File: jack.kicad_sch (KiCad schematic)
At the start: 9 parts

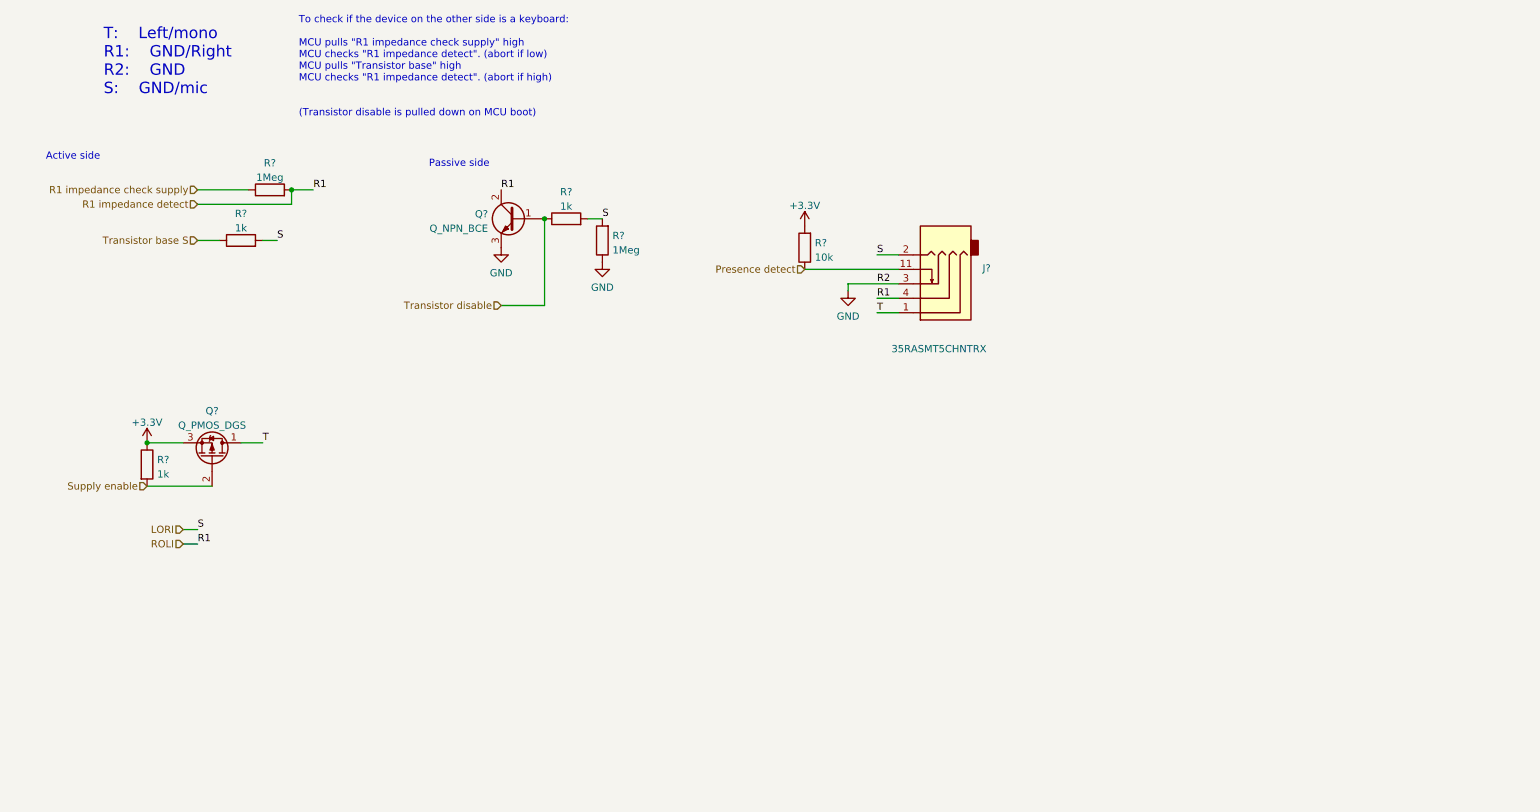
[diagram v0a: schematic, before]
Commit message: Hot pluggable trrs
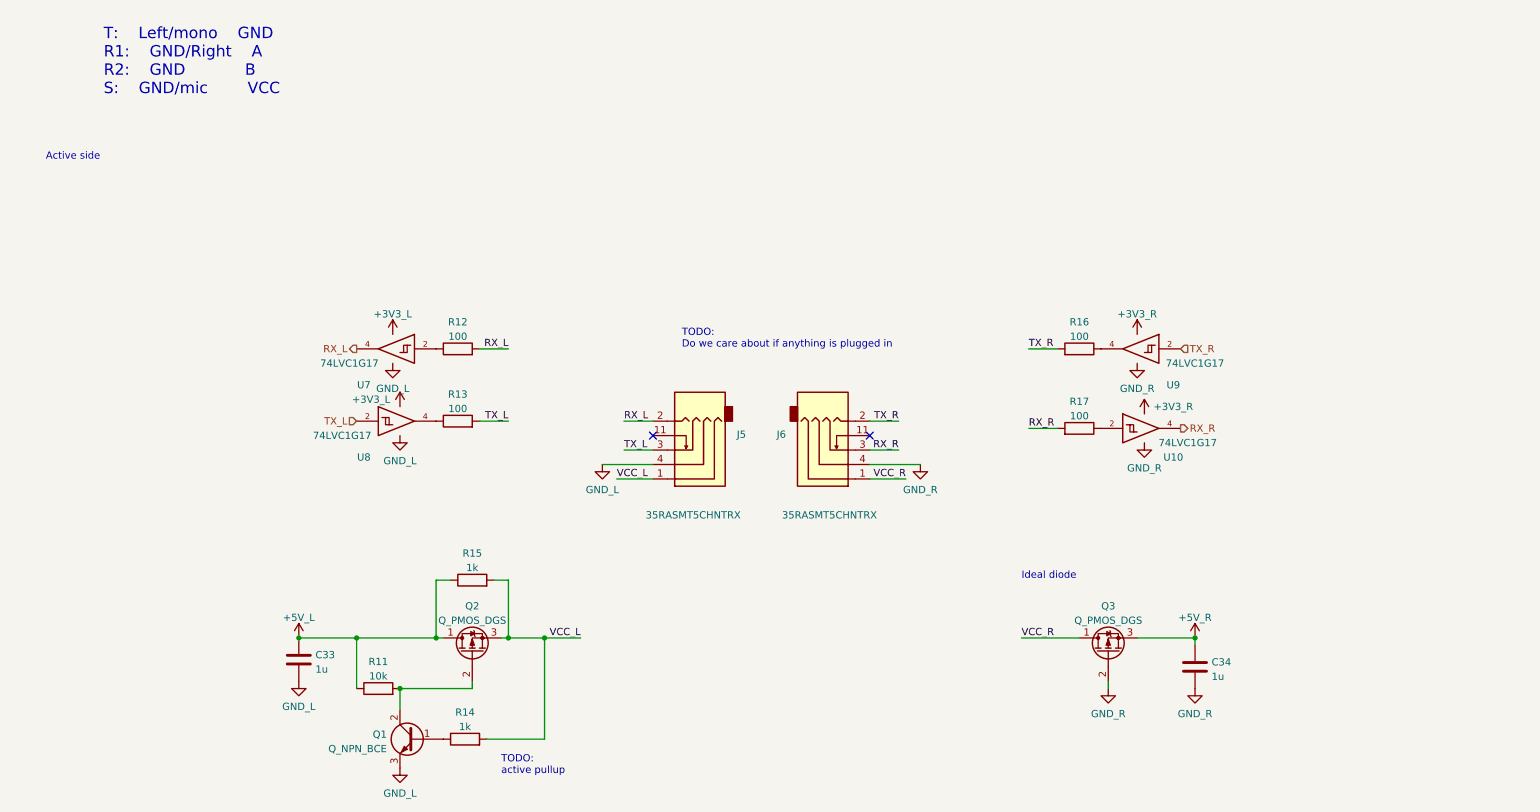
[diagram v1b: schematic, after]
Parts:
- removed Q?: Q_PMOS_DGS, symbol Device:Q_PMOS_DGS
- removed Q?: Q_NPN_BCE, symbol Device:Q_NPN_BCE
- removed R?: 10k, symbol Device:R
- removed R? (x3): 1k, symbol Device:R
- removed R? (x2): 1Meg, symbol Device:R
- added C33, C34: 1u, symbol Device:C
- added J6: 35RASMT5CHNTRX, symbol arisu-split:35RASMT5CHNTRX
- added Q1: Q_NPN_BCE, symbol Device:Q_NPN_BCE
- added Q2, Q3: Q_PMOS_DGS, symbol Device:Q_PMOS_DGS
- added R11: 10k, symbol Device:R
- added R12, R13, R16, R17: 100, symbol Device:R
- added R14, R15: 1k, symbol Device:R
- added U10, U7, U8, U9: 74LVC1G17, symbol 74xGxx:74LVC1G17
- gave numbers to parts that had none: 1
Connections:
- net R1 impedance detect is gone; now on net GND: J5.4
- net GND: now also C33.2, C34.2, J6.4, Q1.3 (E), Q3.2 (G), U10.3 (GND), U7.3 (GND), U8.3 (GND), U9.3 (GND); no longer J5.3
- net LORI renamed RX_L
- net RX_L: now also R12.2, U7.4
- net Presence detect: no longer names the net of J5.11
- net T renamed VCC_L
- net VCC_L: now also Q2.3 (S), R14.2, R15.2
- new net: Q1.1 (B), R14.1
- new net: Q1.2 (C), Q2.2 (G), R11.2
- new net: R16.1, U9.4
- new net: R12.1, U7.2
- new net: R13.1, U8.4
- new net: R17.1, U10.2
- new net +3V3_L: U10.5 (VCC), U7.5 (VCC), U8.5 (VCC), U9.5 (VCC)
- new net +5R: C34.1, Q3.3 (S)
- new net +5V_L: C33.1, Q2.1 (D), R11.1, R15.1
- new net RX_R: J6.3, R17.2, U10.4
- new net TX_L: J5.3, R13.2, U8.2
- new net TX_R: J6.2, R16.2, U9.2
- new net VCC_R: J6.1, Q3.1 (D)
- no-connect marks 0 -> 2
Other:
- note added: "Ideal diode"
- note added: "T: Left/mono GND R1: GND/Right A R2: GND B S: GND/mic VCC"
- note added: "TODO: Do we care about if anything is plugged in"
- note added: "TODO: active pullup"
- note removed: "Passive side"
- note removed: "T: Left/mono R1: GND/Right R2: GND S: GND/mic"
- note removed: "To check if the device on the other side is a keyboard: MCU pulls "R1 impedance check supply" high MCU checks "R1 impedance detect". (abort if low) MCU pulls "Transistor base" high MCU checks "R1 impedance detect". (abort if high) (Transistor disable is pulled down on MCU boot)"
- moved on the sheet: J5

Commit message: No more erc errors + centering and socketing of switches
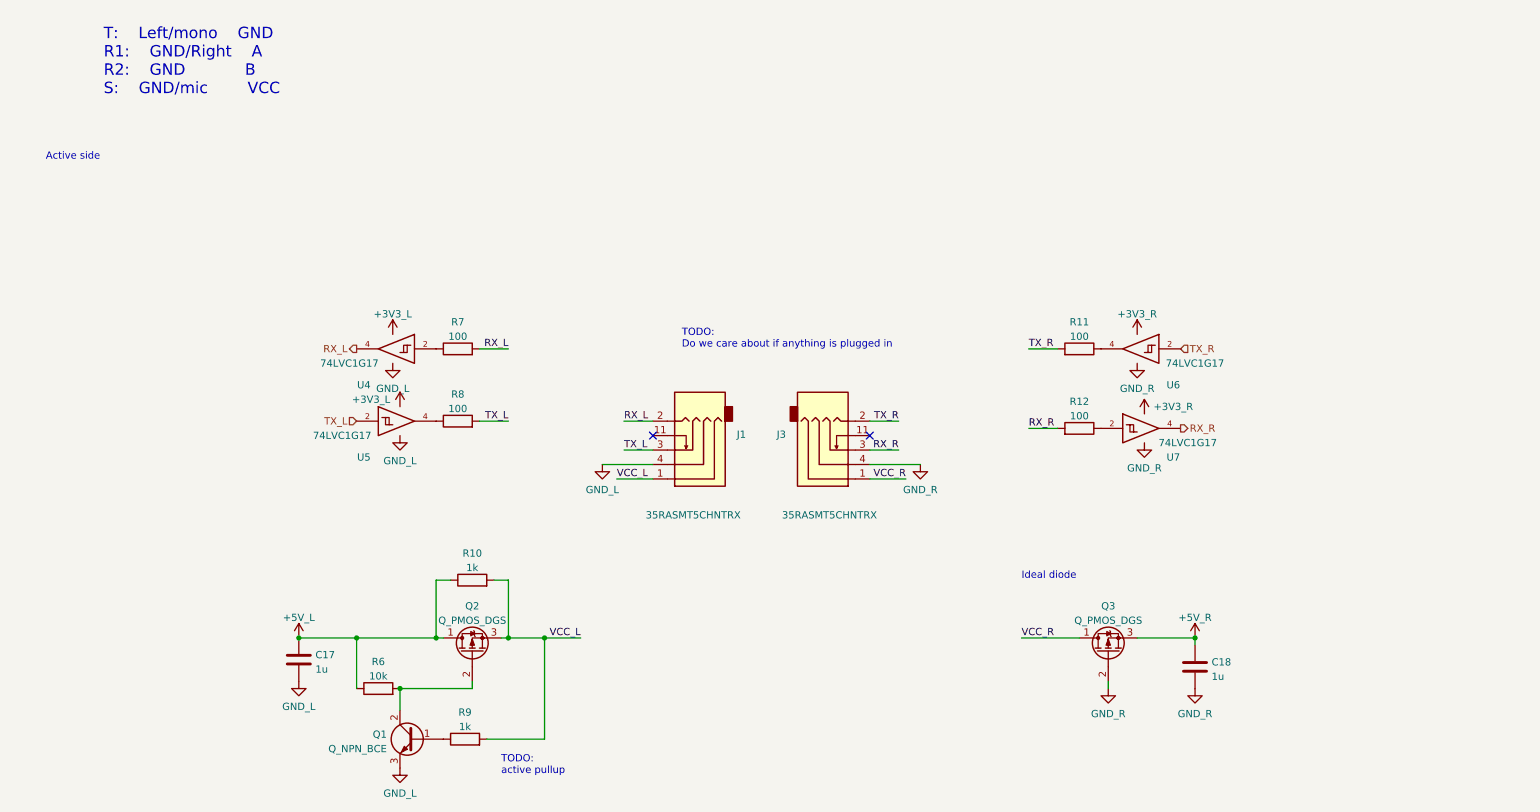
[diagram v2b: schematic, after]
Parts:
- renumbered C33 to C17, C34 to C18, J5 to J1, J6 to J3, R15 to R10, R16 to R11, R17 to R12, R11 to R6, R12 to R7, R13 to R8, R14 to R9, U7 to U4, U8 to U5, U9 to U6, U10 to U7
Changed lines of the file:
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@@
   (symbol (lib_id "Device:C") (at 217.17 134.62 0) (unit 1)
     (in_bom yes) (on_board yes) (fields_autoplaced)
-    (property "Reference" "C34" (id 0) (at 220.091 133.7853 0)
+    (property "Reference" "C18" (id 0) (at 220.091 133.7853 0)
       (effects (font (size 1.27 1.27)) (justify left))
     )
@@
   (symbol (lib_id "Device:C") (at 59.69 133.35 0) (unit 1)
     (in_bom yes) (on_board yes) (fields_autoplaced)
-    (property "Reference" "C33" (id 0) (at 62.611 132.5153 0)
+    (property "Reference" "C17" (id 0) (at 62.611 132.5153 0)
       (effects (font (size 1.27 1.27)) (justify left))
     )
@@
   (symbol (lib_id "arisu-split:+5V_R") (at 217.17 129.54 0) (unit 1)
     (in_bom yes) (on_board yes) (fields_autoplaced)
-    (property "Reference" "#PWR0114" (id 0) (at 217.17 133.35 0)
+    (property "Reference" "#PWR0109" (id 0) (at 217.17 133.35 0)
       (effects (font (size 1.27 1.27)) hide)
     )
@@
   (symbol (lib_id "arisu-split:+3V3_L") (at 77.47 88.9 0) (unit 1)
     (in_bom yes) (on_board yes)
-    (property "Reference" "#PWR0108" (id 0) (at 77.47 92.71 0)
+    (property "Reference" "#PWR0134" (id 0) (at 77.47 92.71 0)
       (effects (font (size 1.27 1.27)) hide)
     )
@@
   (symbol (lib_id "Device:R") (at 90.17 119.38 90) (unit 1)
     (in_bom yes) (on_board yes) (fields_autoplaced)
-    (property "Reference" "R15" (id 0) (at 90.17 114.6642 90))
+    (property "Reference" "R10" (id 0) (at 90.17 114.6642 90))
     (property "Value" "1k" (id 1) (at 90.17 117.2011 90))
     (property "Footprint" "" (id 2) (at 90.17 121.158 90)
@@
   (symbol (lib_id "arisu-split:GND_R") (at 168.91 99.06 0) (unit 1)
     (in_bom yes) (on_board yes) (fields_autoplaced)
-    (property "Reference" "#PWR0111" (id 0) (at 168.91 105.41 0)
+    (property "Reference" "#PWR0107" (id 0) (at 168.91 105.41 0)
       (effects (font (size 1.27 1.27)) hide)
     )
@@
   (symbol (lib_id "Device:R") (at 196.85 78.74 270) (mirror x) (unit 1)
     (in_bom yes) (on_board yes) (fields_autoplaced)
-    (property "Reference" "R16" (id 0) (at 196.85 74.0242 90))
+    (property "Reference" "R11" (id 0) (at 196.85 74.0242 90))
     (property "Value" "100" (id 1) (at 196.85 76.5611 90))
     (property "Footprint" "" (id 2) (at 196.85 80.518 90)
@@
   (symbol (lib_id "Device:R") (at 87.63 78.74 90) (unit 1)
     (in_bom yes) (on_board yes) (fields_autoplaced)
-    (property "Reference" "R12" (id 0) (at 87.63 74.0242 90))
+    (property "Reference" "R7" (id 0) (at 87.63 74.0242 90))
     (property "Value" "100" (id 1) (at 87.63 76.5611 90))
     (property "Footprint" "" (id 2) (at 87.63 80.518 90)
@@
   (symbol (lib_id "arisu-split:+3V3_L") (at 76.2 76.2 0) (unit 1)
     (in_bom yes) (on_board yes)
-    (property "Reference" "#PWR0109" (id 0) (at 76.2 80.01 0)
+    (property "Reference" "#PWR0121" (id 0) (at 76.2 80.01 0)
       (effects (font (size 1.27 1.27)) hide)
     )
@@
   (symbol (lib_id "arisu-split:GND_L") (at 77.47 152.4 0) (unit 1)
     (in_bom yes) (on_board yes) (fields_autoplaced)
-    (property "Reference" "#PWR0106" (id 0) (at 77.47 158.75 0)
+    (property "Reference" "#PWR0115" (id 0) (at 77.47 158.75 0)
       (effects (font (size 1.27 1.27)) hide)
     )
@@
   (symbol (lib_id "arisu-split:GND_L") (at 59.69 137.16 0) (unit 1)
     (in_bom yes) (on_board yes) (fields_autoplaced)
-    (property "Reference" "#PWR0107" (id 0) (at 59.69 143.51 0)
+    (property "Reference" "#PWR0116" (id 0) (at 59.69 143.51 0)
       (effects (font (size 1.27 1.27)) hide)
     )
@@
   (symbol (lib_id "Device:R") (at 87.63 91.44 90) (unit 1)
     (in_bom yes) (on_board yes) (fields_autoplaced)
-    (property "Reference" "R13" (id 0) (at 87.63 86.7242 90))
+    (property "Reference" "R8" (id 0) (at 87.63 86.7242 90))
     (property "Value" "100" (id 1) (at 87.63 89.2611 90))
     (property "Footprint" "" (id 2) (at 87.63 93.218 90)
@@
   (symbol (lib_id "arisu-split:GND_R") (at 208.28 95.25 0) (unit 1)
     (in_bom yes) (on_board yes) (fields_autoplaced)
-    (property "Reference" "#PWR0115" (id 0) (at 208.28 101.6 0)
+    (property "Reference" "#PWR0111" (id 0) (at 208.28 101.6 0)
       (effects (font (size 1.27 1.27)) hide)
     )
@@
   (symbol (lib_id "arisu-split:GND_R") (at 217.17 138.43 0) (unit 1)
     (in_bom yes) (on_board yes) (fields_autoplaced)
-    (property "Reference" "#PWR0112" (id 0) (at 217.17 144.78 0)
+    (property "Reference" "#PWR0108" (id 0) (at 217.17 144.78 0)
       (effects (font (size 1.27 1.27)) hide)
     )
@@
   (symbol (lib_id "74xGxx:74LVC1G17") (at 208.28 92.71 0) (unit 1)
     (in_bom yes) (on_board yes)
-    (property "Reference" "U10" (id 0) (at 213.36 97.79 0))
+    (property "Reference" "U7" (id 0) (at 213.36 97.79 0))
     (property "Value" "74LVC1G17" (id 1) (at 215.9 95.25 0))
     (property "Footprint" "" (id 2) (at 208.28 92.71 0)
@@
   (symbol (lib_id "arisu-split:GND_L") (at 76.2 81.28 0) (unit 1)
     (in_bom yes) (on_board yes) (fields_autoplaced)
-    (property "Reference" "#PWR0134" (id 0) (at 76.2 87.63 0)
+    (property "Reference" "#PWR0120" (id 0) (at 76.2 87.63 0)
       (effects (font (size 1.27 1.27)) hide)
     )
@@
   (symbol (lib_id "Device:R") (at 73.66 138.43 90) (unit 1)
     (in_bom yes) (on_board yes) (fields_autoplaced)
-    (property "Reference" "R11" (id 0) (at 73.66 133.7142 90))
+    (property "Reference" "R6" (id 0) (at 73.66 133.7142 90))
     (property "Value" "10k" (id 1) (at 73.66 136.2511 90))
     (property "Footprint" "" (id 2) (at 73.66 140.208 90)
@@
   (symbol (lib_id "arisu-split:35RASMT5CHNTRX") (at 127 96.52 180) (unit 1)
     (in_bom yes) (on_board yes)
-    (property "Reference" "J5" (id 0) (at 136.652 93.7803 0)
+    (property "Reference" "J1" (id 0) (at 136.652 93.7803 0)
       (effects (font (size 1.27 1.27)) (justify right))
     )
@@
   (symbol (lib_id "arisu-split:+5V_L") (at 59.69 129.54 0) (unit 1)
     (in_bom yes) (on_board yes) (fields_autoplaced)
-    (property "Reference" "#PWR0121" (id 0) (at 59.69 133.35 0)
+    (property "Reference" "#PWR0117" (id 0) (at 59.69 133.35 0)
       (effects (font (size 1.27 1.27)) hide)
     )
@@
   (symbol (lib_id "74xGxx:74LVC1G17") (at 77.47 91.44 0) (unit 1)
     (in_bom yes) (on_board yes)
-    (property "Reference" "U8" (id 0) (at 71.12 97.79 0))
+    (property "Reference" "U5" (id 0) (at 71.12 97.79 0))
     (property "Value" "74LVC1G17" (id 1) (at 67.31 93.98 0))
     (property "Footprint" "" (id 2) (at 77.47 91.44 0)
@@
   (symbol (lib_id "Device:R") (at 88.9 147.32 90) (unit 1)
     (in_bom yes) (on_board yes) (fields_autoplaced)
-    (property "Reference" "R14" (id 0) (at 88.9 142.6042 90))
+    (property "Reference" "R9" (id 0) (at 88.9 142.6042 90))
     (property "Value" "1k" (id 1) (at 88.9 145.1411 90))
     (property "Footprint" "" (id 2) (at 88.9 149.098 90)
@@
   (symbol (lib_id "74xGxx:74LVC1G17") (at 76.2 78.74 0) (mirror y) (unit 1)
     (in_bom yes) (on_board yes)
-    (property "Reference" "U7" (id 0) (at 71.12 85.09 0))
+    (property "Reference" "U4" (id 0) (at 71.12 85.09 0))
     (property "Value" "74LVC1G17" (id 1) (at 68.58 81.28 0))
     (property "Footprint" "" (id 2) (at 76.2 78.74 0)
@@
   (symbol (lib_id "arisu-split:GND_L") (at 113.03 99.06 0) (unit 1)
     (in_bom yes) (on_board yes) (fields_autoplaced)
-    (property "Reference" "#PWR0120" (id 0) (at 113.03 105.41 0)
+    (property "Reference" "#PWR0114" (id 0) (at 113.03 105.41 0)
       (effects (font (size 1.27 1.27)) hide)
     )
@@
   (symbol (lib_id "Device:R") (at 196.85 92.71 270) (mirror x) (unit 1)
     (in_bom yes) (on_board yes) (fields_autoplaced)
-    (property "Reference" "R17" (id 0) (at 196.85 87.9942 90))
+    (property "Reference" "R12" (id 0) (at 196.85 87.9942 90))
     (property "Value" "100" (id 1) (at 196.85 90.5311 90))
     (property "Footprint" "" (id 2) (at 196.85 94.488 90)
@@
   (symbol (lib_id "arisu-split:GND_R") (at 207.01 81.28 0) (unit 1)
     (in_bom yes) (on_board yes) (fields_autoplaced)
-    (property "Reference" "#PWR0117" (id 0) (at 207.01 87.63 0)
+    (property "Reference" "#PWR0113" (id 0) (at 207.01 87.63 0)
       (effects (font (size 1.27 1.27)) hide)
     )
@@
   (symbol (lib_id "arisu-split:GND_R") (at 201.93 138.43 0) (unit 1)
     (in_bom yes) (on_board yes) (fields_autoplaced)
-    (property "Reference" "#PWR0110" (id 0) (at 201.93 144.78 0)
+    (property "Reference" "#PWR0106" (id 0) (at 201.93 144.78 0)
       (effects (font (size 1.27 1.27)) hide)
     )
@@
   (symbol (lib_id "74xGxx:74LVC1G17") (at 207.01 78.74 0) (mirror y) (unit 1)
     (in_bom yes) (on_board yes)
-    (property "Reference" "U9" (id 0) (at 213.36 85.09 0))
+    (property "Reference" "U6" (id 0) (at 213.36 85.09 0))
     (property "Value" "74LVC1G17" (id 1) (at 217.17 81.28 0))
     (property "Footprint" "" (id 2) (at 207.01 78.74 0)
@@
   (symbol (lib_id "arisu-split:+3V3_R") (at 208.28 90.17 0) (unit 1)
     (in_bom yes) (on_board yes)
-    (property "Reference" "#PWR0113" (id 0) (at 208.28 93.98 0)
+    (property "Reference" "#PWR0110" (id 0) (at 208.28 93.98 0)
       (effects (font (size 1.27 1.27)) hide)
     )
@@
   (symbol (lib_id "arisu-split:+3V3_R") (at 207.01 76.2 0) (unit 1)
     (in_bom yes) (on_board yes) (fields_autoplaced)
-    (property "Reference" "#PWR0116" (id 0) (at 207.01 80.01 0)
+    (property "Reference" "#PWR0112" (id 0) (at 207.01 80.01 0)
       (effects (font (size 1.27 1.27)) hide)
     )
@@
   (symbol (lib_id "arisu-split:35RASMT5CHNTRX") (at 154.94 96.52 0) (mirror x) (unit 1)
     (in_bom yes) (on_board yes)
-    (property "Reference" "J6" (id 0) (at 145.288 93.7803 0)
+    (property "Reference" "J3" (id 0) (at 145.288 93.7803 0)
       (effects (font (size 1.27 1.27)) (justify right))
     )
